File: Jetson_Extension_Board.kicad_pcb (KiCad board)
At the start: 2 copper layers, 25 parts, among them J1 I2C_2 DEBUG, J10 TBP03R2-350-03BE, J11 ST DEBUG, J2 TBP03R2-350-03BE, J3 TBP03R2-350-03BE, J4 TBP03R2-350-03BE, J5 TBP03R2-350-03BE, J6 40_Pin_Jetson_Connector, J7 TBP03R2-350-03BE, J8 TBP03R2-350-03BE, J9 TBP03R2-350-03BE, SW1 SW_Push_DPDT, U1 BNO055, U2 74LV14, U4 ADS1115IDGS

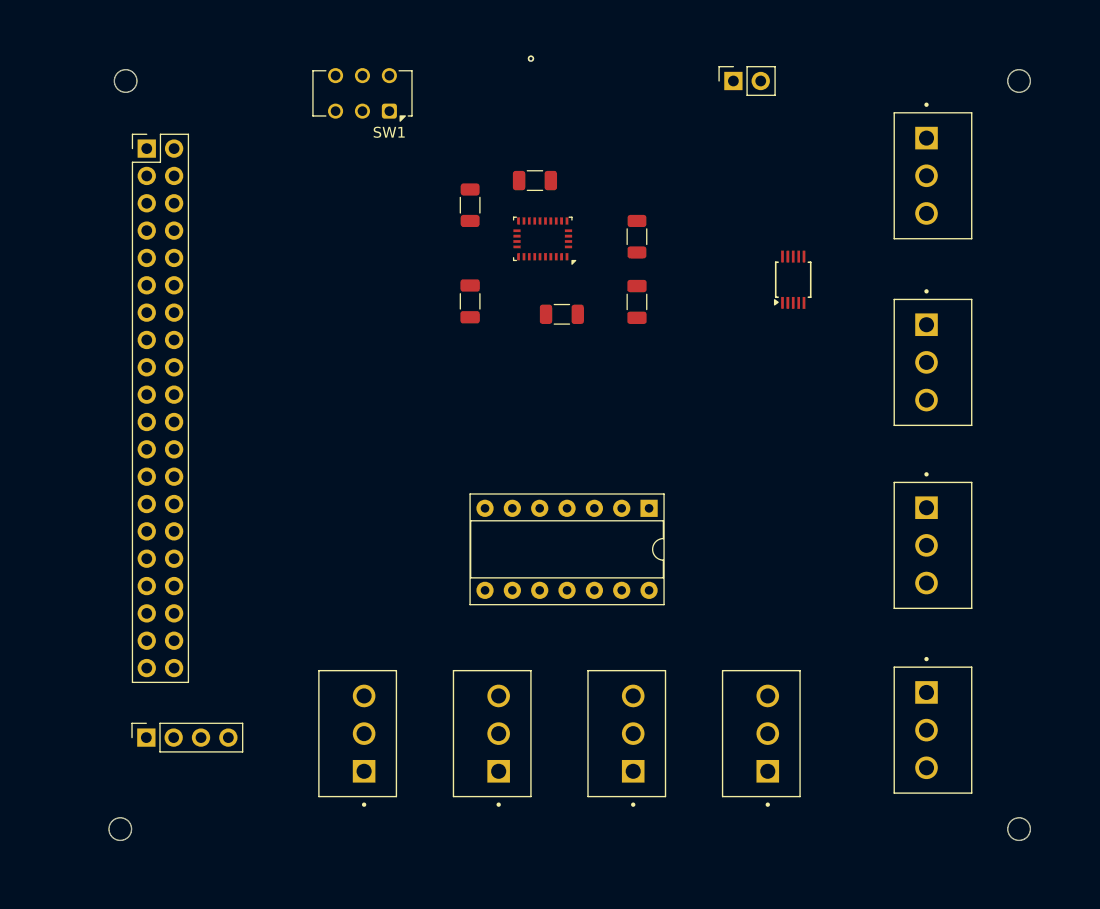
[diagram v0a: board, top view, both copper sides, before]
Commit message: Pluh 1 and 2 removed, main file is updated version
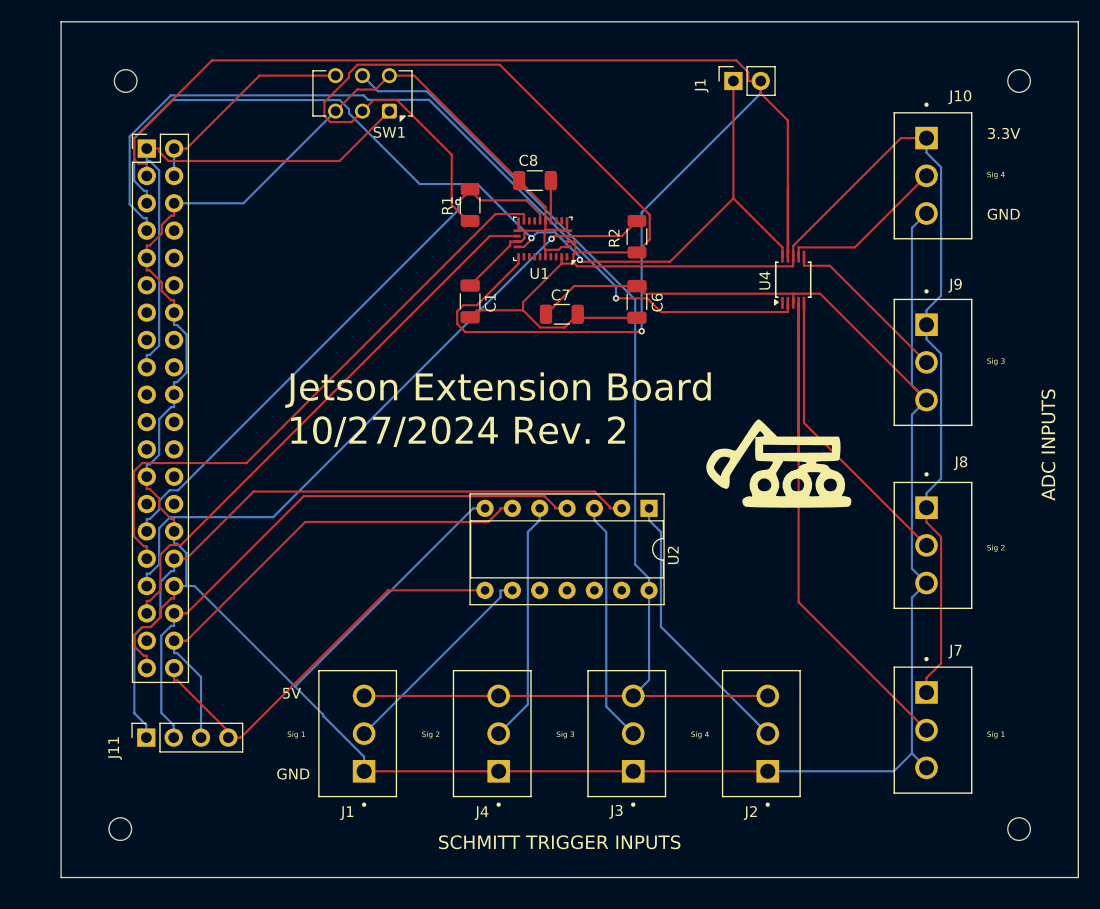
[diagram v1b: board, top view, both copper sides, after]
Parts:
- added G***: LOGO, LOGO, F.Cu at (155.5, 109.0)
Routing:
- net GND: track 0.00 -> 319.8 mm
- net /ADC/3.3V: track 0.00 -> 191.9 mm
- net /I2C_2_SDA: track 0.00 -> 145.2 mm, vias 0 -> 1
- net /SchmittTrigger(74LV14)/5V: track 0.00 -> 110.5 mm
- net /I2C_2_SCL: track 0.00 -> 93.7 mm, vias 0 -> 2
- net ADC ALERT: track 0.00 -> 82.6 mm, vias 0 -> 1
- net ST 1: track 0.00 -> 64.1 mm
- net IMU nBOOT: track 0.00 -> 62.2 mm, vias 0 -> 1
- net /ADC/Signal 1: track 0.00 -> 58.5 mm
- net IMU INT: track 0.00 -> 55.5 mm
- net ST 2: track 0.00 -> 54.2 mm
- net IMU nRESET: track 0.00 -> 52.9 mm, vias 0 -> 1
- net COM 3: track 0.00 -> 51.5 mm
- net ST 3: track 0.00 -> 46.8 mm
- net 3.3V: track 0.00 -> 46.7 mm
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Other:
- board outline added: 94.5 x 79.5 mm
- board text added: "3.3V"
- board text added: "5V"
- board text added: "ADC INPUTS"
- board text added: "C1"
- board text added: "C6"
- board text added: "C7"
- board text added: "C8"
- board text added: "GND"
- board text added: "J1"
- board text added: "J10"
- board text added: "J11"
- board text added: "J2"
- board text added: "J3"
- board text added: "J4"
- board text added: "J7"
- board text added: "J8"
- board text added: "J9"
- board text added: "Jetson Extension Board 10/27/2024 Rev. 2"
- board text added: "R1"
- board text added: "R2"
- board text added: "SCHMITT TRIGGER INPUTS"
- board text added: "Sig 1"
- board text added: "Sig 2"
- board text added: "Sig 3"
- board text added: "Sig 4"
- board text added: "U1"
- board text added: "U2"
- board text added: "U4"

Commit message: LEDS
consolidated file, added diode and resistor (look over), and silkscreen errors present
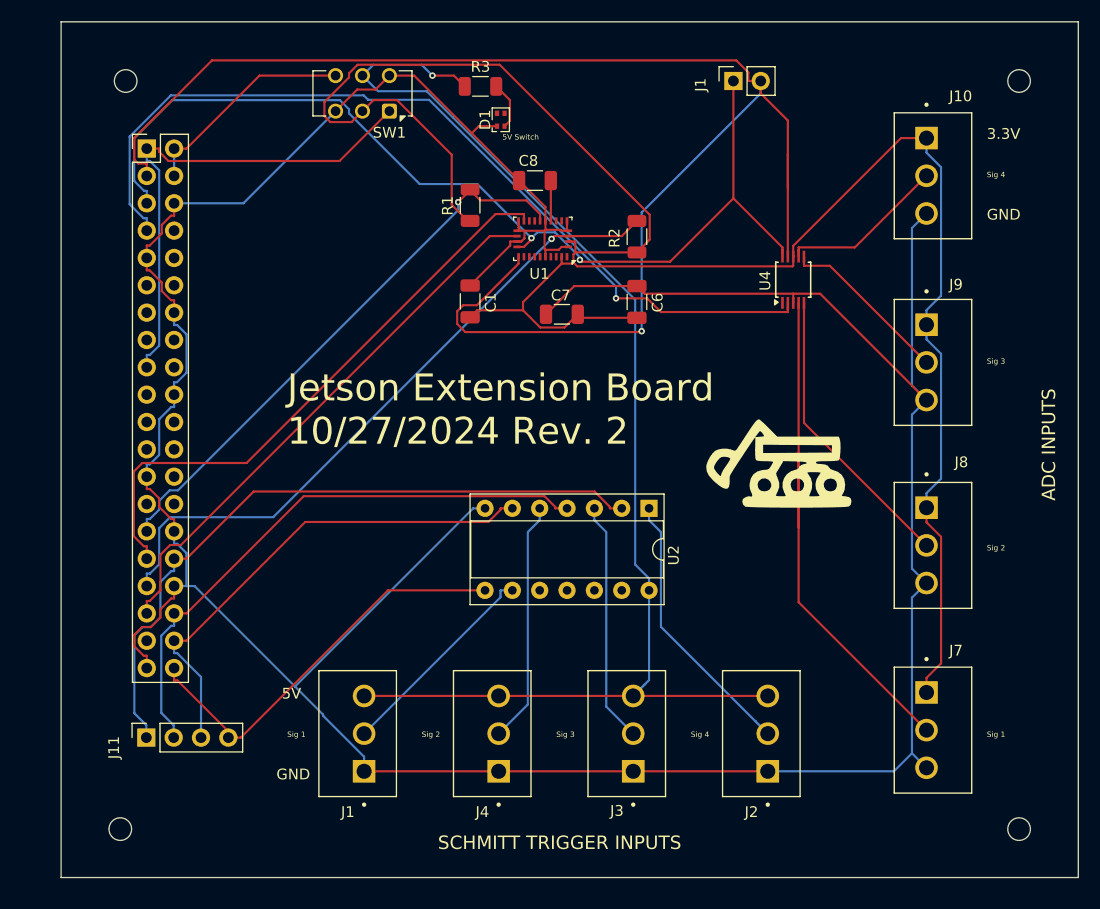
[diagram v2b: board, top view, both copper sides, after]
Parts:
- added D1: D, LED_SMD:LED_LiteOn_LTST-C295K_1.6x0.8mm, F.Cu at (129.3, 76.6)
- added R3: 150, Resistor_SMD:R_1206_3216Metric, F.Cu at (127.5, 73.5)
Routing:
- net /SchmittTrigger(74LV14)/5V: track 110.5 -> 120.7 mm, vias 0 -> 1
- net /ADC/Signal 1: track 58.5 -> 51.6 mm
- net /ADC/Signal 2: track 32.8 -> 27.2 mm
- net Net-(D1-A): track 0.00 -> 4.44 mm
- net /I2C_2_SDA: track 145.2 -> 142.1 mm
- net GND: track 319.8 -> 322.5 mm
- net Net-(J2-Pad2): track 27.2 -> 28.0 mm
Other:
- board text added: "5V Switch"

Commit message: Added Correct LED
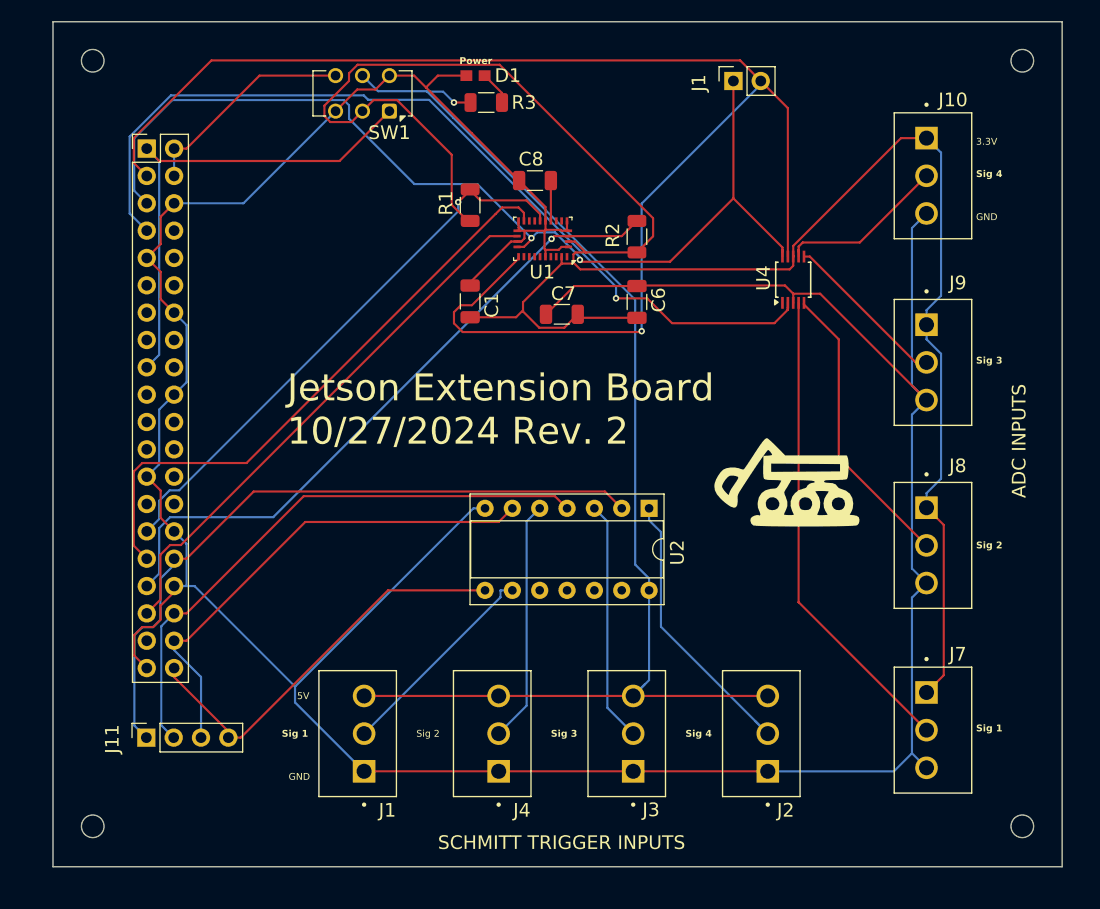
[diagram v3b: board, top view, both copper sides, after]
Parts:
- D1: value D -> LTST-C191KGKT; footprint LED_SMD:LED_LiteOn_LTST-C295K_1.6x0.8mm -> LTST_C191KGKT:0603
- H1: moved to F.Cu
- R3: value 150 -> 260
- moved D1 4.73 mm to (127.0, 72.5), turned to 0 degrees
- moved H1 3.59 mm to (91.4, 71.1), turned to 0 degrees
- moved H2 2.57 mm to (91.4, 142.2)
- moved G*** 1.90 mm to (156.2, 110.8)
- moved H3 1.90 mm to (177.8, 71.1)
- moved R3 1.59 mm to (128.0, 75.0)
- moved H4 0.40 mm to (177.8, 142.2)
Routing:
- net /ADC/Signal 1: track 51.6 -> 44.6 mm
- net /SchmittTrigger(74LV14)/5V: track 120.7 -> 114.4 mm
- net /I2C_2_SDA: track 142.1 -> 138.3 mm
- net Net-(D1-Pad2): track 4.44 -> 3.17 mm
- net /ADC/3.3V: track 191.9 -> 193.1 mm
- net /ADC/Signal 3: track 16.2 -> 15.5 mm
- net ADC ALERT: track 82.3 -> 82.9 mm
- net 3.3V: track 46.7 -> 46.2 mm
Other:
- board size 94.5 x 79.5 mm -> 93.8 x 78.5 mm
- board text added: "Power"
- board text removed: "5V Switch"

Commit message: Edited silkscreen
Added labels for debug pins
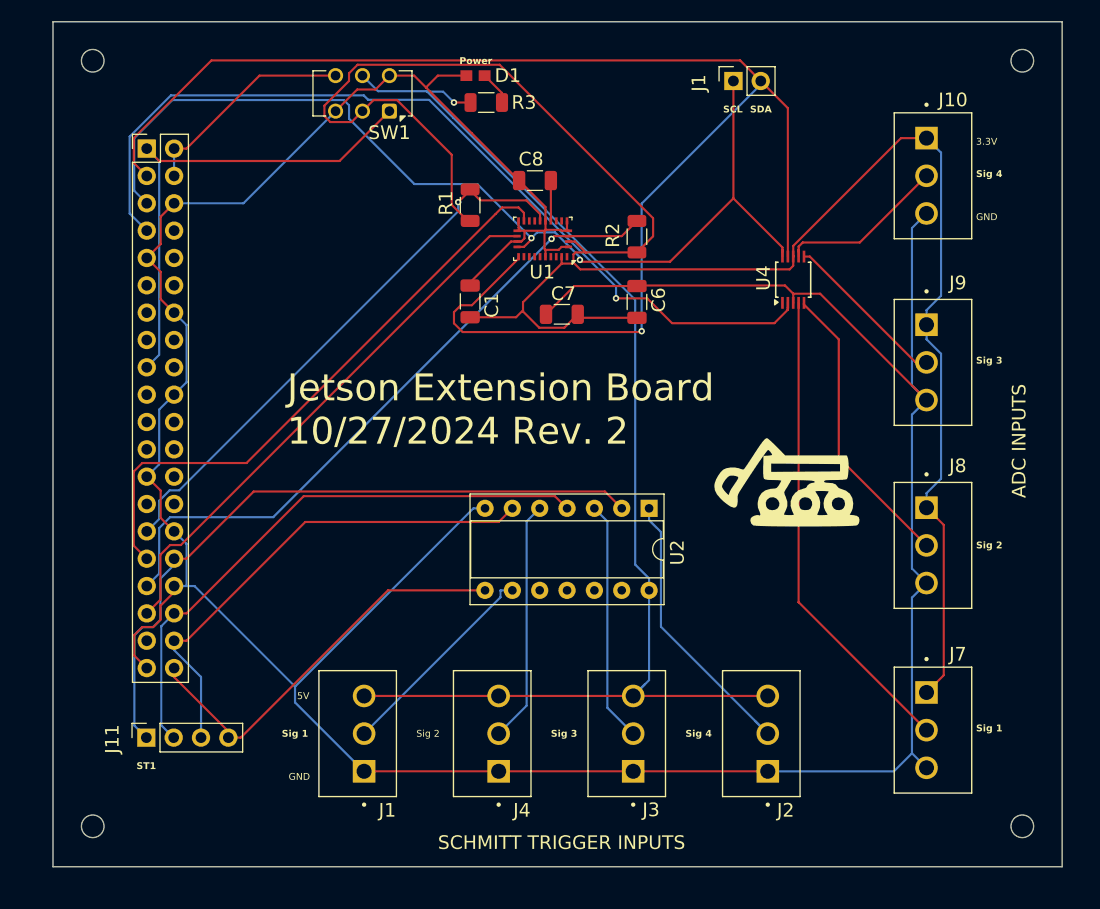
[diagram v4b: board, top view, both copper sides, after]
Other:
- board text added: "SCL"
- board text added: "SDA"
- board text added: "ST1"
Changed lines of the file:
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@@
+		)
+	)
+	(gr_text "ST1"
+		(at 95.5 137 0)
+		(layer "F.SilkS")
+		(effects
+			(font
+				(size 0.635 0.635)
+				(thickness 0.127)
+				(bold yes)
+			)
+			(justify left bottom)
 		)
 	)
@@
 		)
 	)
+	(gr_text "SCL"
+		(at 150 76 0)
+		(layer "F.SilkS")
+		(effects
+			(font
+				(size 0.635 0.635)
+				(thickness 0.127)
+				(bold yes)
+			)
+			(justify left bottom)
+		)
+	)
 	(gr_text "Sig 4"
 		(at 146.5 134 0)
@@
 			)
 			(justify left bottom)
+		)
+	)
+	(gr_text "SDA"
+		(at 152.5 76 0)
+		(layer "F.SilkS")
+		(effects
+			(font
+				(size 0.635 0.635)
+				(thickness 0.127)
+				(bold yes)
+			)
+			(justify left bottom)

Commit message: PCB Update
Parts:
- removed C1: 120n, Capacitor_SMD:C_1206_3216Metric
- removed C6, C8: 100n, Capacitor_SMD:C_1206_3216Metric
- removed C7: 6.8n, Capacitor_SMD:C_1206_3216Metric
- removed R1, R2: 10k, Resistor_SMD:R_1206_3216Metric
- removed U1: BNO055, Package_LGA:LGA-28_5.2x3.8mm_P0.5mm
- added C2: 0.1u, Capacitor_SMD:C_1206_3216Metric, F.Cu at (134.5, 109.0)
- added J12: TBP03R2-350-03BE, TBP03R2_350_03BE(1):CUI_TBP03R2-350-03BE, F.Cu at (150.8, 137.7)
- added J13: TBP03R2-350-03BE, TBP03R2_350_03BE(1):CUI_TBP03R2-350-03BE, F.Cu at (159.6, 137.7)
- added J14: Conn_01x06_Pin, Connector_JST:JST_EH_B6B-EH-A_1x06_P2.50mm_Vertical, F.Cu at (112.7, 95.8)
- added J15: Conn_01x04_Pin, Connector_JST:JST_EH_B4B-EH-A_1x04_P2.50mm_Vertical, F.Cu at (130.5, 93.2)
- J11: footprint Connector_PinSocket_2.54mm:PinSocket_1x04_P2.54mm_Vertical -> Connector_JST:JST_EH_B6B-EH-A_1x06_P2.50mm_Vertical
- R3: value 260 -> 270
- moved J6 49.2 mm to (104.0, 127.9), turned to 180 degrees
- moved SW1 35.0 mm to (154.0, 77.5)
- moved U4 16.7 mm to (140.0, 89.0)
- moved J7 15.2 mm to (160.9, 116.8)
- moved J8 12.4 mm to (160.5, 103.5)
- moved J2 11.6 mm to (142.6, 137.6)
- moved J1 10.5 mm to (141.2, 77.0)
- moved J9 9.93 mm to (160.5, 90.3)
- moved D1 8.73 mm to (135.5, 74.5)
- moved J10 8.50 mm to (160.5, 77.0)
- moved J3 8.15 mm to (133.5, 137.2)
- moved R3 8.08 mm to (135.5, 78.0)
- moved J4 4.15 mm to (125.0, 137.2)
- moved J11 3.80 mm to (92.8, 135.0), turned to 0 degrees
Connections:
- J11 pad 1: ST 1 -> /SchmittTrigger(74LV14)/ST 6
- J11 pad 2: ST 2 -> /SchmittTrigger(74LV14)/ST 5
- J11 pad 3: ST 3 -> ST 4
- J11 pad 4: ST 4 -> ST 3
- J6 pad 33: IMU nBOOT -> unconnected-(J6-Pin_33-Pad33)
- SW1 pad 1: 3.3V -> GND
- SW1 pad 3: GND -> 3.3V
- U2 pad 10: unconnected-(U2-Pad10) -> /SchmittTrigger(74LV14)/ST 5
- U2 pad 12: unconnected-(U2-Pad12) -> /SchmittTrigger(74LV14)/ST 6
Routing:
- net GND: track 322.1 -> 600.9 mm, vias 0 -> 4
- net COM 3: track 51.4 -> 220.8 mm, vias 0 -> 3
- net 3.3V: track 46.2 -> 145.5 mm, vias 0 -> 5
- net ADC ALERT: track 82.9 -> 0.00 mm, vias 1 -> 0
- net /I2C_2_SCL: track 93.8 -> 173.5 mm
- net Net-(D1-Pad2): track 3.17 -> 77.6 mm, vias 0 -> 1
- net ST 4: track 38.3 -> 106.7 mm, vias 0 -> 3
- net IMU nBOOT: track 62.1 -> 0.00 mm, vias 1 -> 0
- net /SchmittTrigger(74LV14)/5V: track 114.4 -> 170.8 mm, vias 1 -> 2
- net unconnected-(J6-Pin_33-Pad33): track 0.00 -> 54.7 mm
- net ST 1: track 64.0 -> 118.4 mm, vias 0 -> 3
- net /I2C_2_SDA: track 138.3 -> 192.2 mm, vias 1 -> 3
- net ST 2: track 54.0 -> 107.1 mm, vias 0 -> 3
- net /SchmittTrigger(74LV14)/ST 6: track 0.00 -> 52.9 mm
- net /SchmittTrigger(74LV14)/ST 5: track 0.00 -> 45.2 mm
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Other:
- board text removed: "C1"
- board text removed: "C6"
- board text removed: "C7"
- board text removed: "J11"
- board text removed: "R1"
- board text removed: "R2"
- board text removed: "U1"
